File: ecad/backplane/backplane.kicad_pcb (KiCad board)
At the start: 2 copper layers, 18 parts, among them J1 10145891-0320J13LF, J2 10145891-0320J13LF, J3 10145891-0320J13LF, J4 10145891-0320J13LF, J6 USB4105-GF-A, U1 MCP16331x-xCH

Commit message: hii
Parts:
- moved R4 37.5 mm to (34.0, 106.9)
- moved J6 37.5 mm to (32.9, 115.2)
- moved R3 37.5 mm to (31.5, 106.9)
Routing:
- net GND: track 97.9 -> 112.7 mm, vias 6 -> 8
- net +5V: track 6.47 -> 18.3 mm
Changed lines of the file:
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@@
 			(effects
 				(font
-					(size 1 1)
-					(thickness 0.15)
+					(size 0.5 0.5)
+					(thickness 0.125)
 				)
 			)
@@
 			(effects
 				(font
-					(size 1 1)
-					(thickness 0.15)
+					(size 0.3 0.3)
+					(thickness 0.075)
 				)
 			)
@@
 			(effects
 				(font
-					(size 1 1)
-					(thickness 0.15)
+					(size 0.3 0.3)
+					(thickness 0.075)
 				)
 			)
@@
 			(effects
 				(font
-					(size 1 1)
-					(thickness 0.15)
+					(size 0.3 0.3)
+					(thickness 0.075)
 				)
 			)
@@
 			(effects
 				(font
-					(size 1 1)
-					(thickness 0.15)
+					(size 0.3 0.3)
+					(thickness 0.075)
 				)
 			)
@@
 			(effects
 				(font
-					(size 1 1)
-					(thickness 0.15)
+					(size 0.3 0.3)
+					(thickness 0.075)
 				)
 			)
@@
 	(footprint "Resistor_SMD:R_0402_1005Metric"
 		(layer "F.Cu")
-		(at 68.85 103.5 90)
+		(at 31.4625 106.87 90)
 		(descr "Resistor SMD 0402 (1005 Metric), square (rectangular) end terminal, IPC_7351 nominal, (Body size source: IPC-SM-782 page 72, https://www.pcb-3d.com/wordpress/wp-content/uploads/ipc-sm-782a_amendment_1_and_2.pdf), generated with kicad-footprint-generator")
 		(tags "resistor")
@@
 			(effects
 				(font
-					(size 1 1)
-					(thickness 0.15)
+					(size 0.3 0.3)
+					(thickness 0.075)
 				)
 			)
@@
 			(effects
 				(font
-					(size 1 1)
-					(thickness 0.15)
+					(size 0.3 0.3)
+					(thickness 0.075)
 				)
 			)
@@
 	(footprint "Resistor_SMD:R_0402_1005Metric"
 		(layer "F.Cu")
-		(at 71.4 103.5 90)
+		(at 34.0125 106.87 90)
 		(descr "Resistor SMD 0402 (1005 Metric), square (rectangular) end terminal, IPC_7351 nominal, (Body size source: IPC-SM-782 page 72, https://www.pcb-3d.com/wordpress/wp-content/uploads/ipc-sm-782a_amendment_1_and_2.pdf), generated with kicad-footprint-generator")
 		(tags "resistor")
@@
 	(footprint "Library:GCT_USB4105-GF-A"
 		(layer "F.Cu")
-		(at 70.2875 111.785)
+		(at 32.9 115.155)
 		(property "Reference" "J6"
 			(at -1.825 -8.635 0)
@@
 	)
 	(segment
+		(start 35.3 110.4)
+		(end 35.3 107.55)
+		(width 0.2)
+		(layer "F.Cu")
+		(net 898)
+	)
+	(segment
 		(start 45.3375 100.0625)
 		(end 44.2 101.2)
@@
 	)
 	(segment
-		(start 68.85 102.99)
-		(end 71.4 102.99)
+		(start 35.3 107.55)
+		(end 41.65 101.2)
+		(width 0.2)
+		(layer "F.Cu")
+		(net 898)
+	)
+	(segment
+		(start 31.4625 106.36)
+		(end 34.0125 106.36)
 		(width 0.2)
 		(layer "F.Cu")
@@
 	)
 	(segment
-		(start 67.0875 107.03)
-		(end 67.0875 104.7525)
+		(start 29.7 110.4)
+		(end 29.7 108.1225)
+		(width 0.2)
+		(layer "F.Cu")
+		(net 899)
+	)
+	(segment
+		(start 35.14 106.36)
+		(end 35.7 105.8)
+		(width 0.2)
+		(layer "F.Cu")
+		(net 899)
+	)
+	(segment
+		(start 36.1 107.95)
+		(end 36.1 110.4)
 		(width 0.2)
 		(layer "F.Cu")
@@
 	)
 	(segment
-		(start 74.0325 107.03)
-		(end 74.6075 107.605)
+		(start 36.645 110.4)
+		(end 37.22 110.975)
+		(width 0.2)
+		(layer "F.Cu")
+		(net 899)
+	)
+	(segment
+		(start 38.25 105.8)
+		(end 41.65 102.4)
 		(width 0.2)
 		(layer "F.Cu")
@@
 	)
 	(segment
-		(start 67.0875 104.7525)
-		(end 68.85 102.99)
+		(start 29.7 108.1225)
+		(end 31.4625 106.36)
 		(width 0.2)
 		(layer "F.Cu")
@@
 	)
 	(segment
-		(start 65.9675 107.605)
-		(end 66.5125 107.605)
+		(start 28.58 110.975)
+		(end 29.125 110.975)
 		(width 0.2)
 		(layer "F.Cu")
@@
 	)
 	(segment
-		(start 73.4875 107.03)
-		(end 74.0325 107.03)
+		(start 36.1 110.4)
+		(end 36.645 110.4)
 		(width 0.2)
 		(layer "F.Cu")
@@
 	)
 	(segment
+		(start 41.65 102.4)
+		(end 41.65 102.335)
+		(width 0.2)
+		(layer "F.Cu")
+		(net 899)
+	)
+	(segment
 		(start 46.515 104.65)
 		(end 44.2 102.335)
@@
 	)
 	(segment
-		(start 66.5125 107.605)
-		(end 67.0875 107.03)
+		(start 38.25 105.8)
+		(end 36.1 107.95)
+		(width 0.2)
+		(layer "F.Cu")
+		(net 899)
+	)
+	(segment
+		(start 34.0125 106.36)
+		(end 35.14 106.36)
+		(width 0.2)
+		(layer "F.Cu")
+		(net 899)
+	)
+	(segment
+		(start 29.125 110.975)
+		(end 29.7 110.4)
 		(width 0.2)
 		(layer "F.Cu")
@@
 	)
 	(via
+		(at 38.25 105.8)
+		(size 0.6)
+		(drill 0.3)
+		(layers "F.Cu" "B.Cu")
+		(net 899)
+	)
+	(via
 		(at 49.3 100.05)
 		(size 0.6)
@@
 	)
 	(via
+		(at 35.7 105.8)
+		(size 0.6)
+		(drill 0.3)
+		(layers "F.Cu" "B.Cu")
+		(net 899)
+	)
+	(via
 		(at 64.6 83.95)
 		(size 0.6)
@@
 	)
 	(segment
+		(start 35.7 105.8)
+		(end 38.25 105.8)
+		(width 0.2)
+		(layer "B.Cu")
+		(net 899)
+	)
+	(segment
 		(start 64.6 35.65)
 		(end 64.6 51.75)
@@
 	)
 	(segment
-		(start 69.5375 107.03)
-		(end 69.5375 104.6975)
+		(start 32.15 110.4)
+		(end 32.15 108.0675)
 		(width 0.2)
 		(layer "F.Cu")
@@
 	)
 	(segment
-		(start 69.5375 104.6975)
-		(end 68.85 104.01)
+		(start 32.15 108.0675)
+		(end 31.4625 107.38)
 		(width 0.2)
 		(layer "F.Cu")
@@
 	)
 	(segment
-		(start 71.0375 107.03)
-		(end 71.0375 104.3725)
+		(start 33.65 110.4)
+		(end 33.65 107.7425)
 		(width 0.2)
 		(layer "F.Cu")
@@
 	)
 	(segment
-		(start 71.0375 104.3725)
-		(end 71.4 104.01)
+		(start 33.65 107.7425)
+		(end 34.0125 107.38)
 		(width 0.2)
 		(layer "F.Cu")
@@
 		(min_thickness 0.25)
 		(filled_areas_thickness no)
-		(fill yes
+		(fill
 			(thermal_gap 0.5)
 			(thermal_bridge_width 0.5)
@@
 		(polygon
 			(pts
-				(xy 198.05 19.55) (xy 23.8 20.7) (xy 22.95 109.25) (xy 22.95 117.3) (xy 198.05 116.15)
+				(xy 191.25 20.7) (xy 23.8 20.7) (xy 22.95 109.25) (xy 22.95 117.3) (xy 191.25 117.3)
 			)
 		)

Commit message: various changes
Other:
- board outline added: 220 x 160 mm
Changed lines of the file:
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@@
 		)
+	)
+	(gr_rect
+		(start -5.1 -27.45)
+		(end 214.9 132.55)
+		(stroke
+			(width 0.2)
+			(type default)
+		)
+		(fill none)
+		(layer "Edge.Cuts")
 	)
 	(segment

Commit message: fix backplane pins
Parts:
- moved J6 197.6 mm to (214.0, 36.0), turned to 180 degrees
- moved R3 194.3 mm to (215.4, 44.3), turned to -90 degrees
- moved R4 189.5 mm to (212.9, 44.3), turned to -90 degrees
- moved CIn_2 171.8 mm to (205.2, 49.4), turned to 90 degrees
- moved CIn_1 166.9 mm to (202.7, 49.4), turned to 90 degrees
- moved RBot 165.0 mm to (204.4, 59.8), turned to 90 degrees
- moved C4 163.0 mm to (198.2, 43.1), turned to 0 degrees
- moved U1 161.8 mm to (201.6, 54.6), turned to 90 degrees
- moved C5 160.3 mm to (198.2, 46.5), turned to 0 degrees
- moved RTop 160.0 mm to (201.8, 59.8), turned to 90 degrees
- moved D1 154.2 mm to (196.8, 51.7), turned to 90 degrees
- moved CB 153.5 mm to (197.6, 55.8), turned to -90 degrees
- moved DB 147.0 mm to (194.2, 55.8), turned to -90 degrees
- moved L 146.1 mm to (192.5, 51.7), turned to 90 degrees
- moved J1 116.0 mm to (104.8, 146.8), turned to 90 degrees
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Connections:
- net /ADDR00 renamed /BUS42
- net /ADDR02 renamed /BUS43
- net /ADDR04 renamed /BUS44
- net /ADDR06 renamed /BUS45
- net /ADDR08 renamed /BUS48
- net /BUS00 renamed /BUS54
- net /BUS02 renamed /BUS55
- net /BUS04 renamed /BUS56
- net /BUS15 renamed /BUS24
- net /BUS16 renamed /BUS66
- net /DATA00 renamed /BUS72
- net /DATA01 renamed /BUS33
- net /DATA03 renamed /BUS34
- net /DATA05 renamed /BUS35
- net /DATA07 renamed /BUS36
- J1 pad 10: /ADDR11 -> /BUS10
- J1 pad 11: /ADDR13 -> /BUS11
- J1 pad 12: /ADDR15 -> /BUS12
- J1 pad 14: GND -> 3.3V
- J1 pad 15: /BUS01 -> GND
- J1 pad 16: /BUS03 -> GND
- J1 pad 17: /BUS05 -> /BUS17
- J1 pad 18: /BUS07 -> /BUS18
- J1 pad 19: 3.3V -> /BUS19
- J1 pad 2: GND -> 3.3V
- J1 pad 20: GND -> /BUS20
- J1 pad 21: /BUS09 -> /BUS21
- J1 pad 22: /BUS11 -> /BUS22
- J1 pad 23: /BUS13 -> /BUS23
- J1 pad 26: GND -> 3.3V
- J1 pad 27: /BUS17 -> GND
- J1 pad 28: /BUS19 -> GND
- J1 pad 29: /BUS21 -> /BUS29
- J1 pad 3: /ADDR01 -> GND
- J1 pad 30: /BUS23 -> /BUS30
- J1 pad 31: 3.3V -> /BUS31
- J1 pad 32: GND -> /BUS32
- J1 pad 38: GND -> 3.3V
- J1 pad 39: unconnected-(J1-Pad39) -> GND
- J1 pad 4: /ADDR03 -> GND
- J1 pad 40: 3.3V -> GND
- J1 pad 41: GND -> /BUS41
- J1 pad 46: 3.3V -> /BUS46
- J1 pad 47: GND -> /BUS47
- J1 pad 49: /ADDR10 -> 3.3V
- J1 pad 5: /ADDR05 -> /BUS05
- J1 pad 50: /ADDR12 -> 3.3V
- J1 pad 51: /ADDR14 -> GND
- J1 pad 52: 3.3V -> GND
- J1 pad 53: GND -> /BUS53
- J1 pad 57: /BUS06 -> /BUS57
- J1 pad 58: 3.3V -> /BUS58
- J1 pad 59: GND -> /BUS59
- J1 pad 6: /ADDR07 -> /BUS06
- J1 pad 60: /BUS08 -> /BUS60
- J1 pad 61: /BUS10 -> 3.3V
- J1 pad 62: /BUS12 -> 3.3V
- J1 pad 63: /BUS14 -> GND
- J1 pad 64: 3.3V -> GND
- J1 pad 65: GND -> /BUS65
- J1 pad 67: /BUS18 -> /BUS67
- J1 pad 68: /BUS20 -> /BUS68
- J1 pad 69: /BUS22 -> /BUS69
- J1 pad 7: 3.3V -> /BUS07
- J1 pad 70: 3.3V -> /BUS70
- J1 pad 71: GND -> /BUS71
- J1 pad 73: /DATA02 -> 3.3V
- J1 pad 74: /DATA04 -> 3.3V
- J1 pad 75: /DATA06 -> GND
- J1 pad 76: 3.3V -> GND
- J1 pad 77: GND -> unconnected-(J1-Pad77)
- J1 pad 8: GND -> /BUS08
- J1 pad 9: /ADDR09 -> /BUS09
- J2 pad 10: /ADDR11 -> /BUS10
- J2 pad 11: /ADDR13 -> /BUS11
- J2 pad 12: /ADDR15 -> /BUS12
- J2 pad 14: GND -> 3.3V
- J2 pad 15: /BUS01 -> GND
- J2 pad 16: /BUS03 -> GND
- J2 pad 17: /BUS05 -> /BUS17
- J2 pad 18: /BUS07 -> /BUS18
- J2 pad 19: 3.3V -> /BUS19
- J2 pad 2: GND -> 3.3V
- J2 pad 20: GND -> /BUS20
- J2 pad 21: /BUS09 -> /BUS21
- J2 pad 22: /BUS11 -> /BUS22
- J2 pad 23: /BUS13 -> /BUS23
- J2 pad 26: GND -> 3.3V
- J2 pad 27: /BUS17 -> GND
- J2 pad 28: /BUS19 -> GND
- J2 pad 29: /BUS21 -> /BUS29
- J2 pad 3: /ADDR01 -> GND
- J2 pad 30: /BUS23 -> /BUS30
- J2 pad 31: 3.3V -> /BUS31
- J2 pad 32: GND -> /BUS32
- J2 pad 38: GND -> 3.3V
- J2 pad 39: unconnected-(J2-Pad39) -> GND
- J2 pad 4: /ADDR03 -> GND
- J2 pad 40: 3.3V -> GND
- J2 pad 41: GND -> /BUS41
- J2 pad 46: 3.3V -> /BUS46
- J2 pad 47: GND -> /BUS47
- J2 pad 49: /ADDR10 -> 3.3V
- J2 pad 5: /ADDR05 -> /BUS05
- J2 pad 50: /ADDR12 -> 3.3V
- J2 pad 51: /ADDR14 -> GND
- J2 pad 52: 3.3V -> GND
- J2 pad 53: GND -> /BUS53
- J2 pad 57: /BUS06 -> /BUS57
- J2 pad 58: 3.3V -> /BUS58
- J2 pad 59: GND -> /BUS59
- J2 pad 6: /ADDR07 -> /BUS06
- J2 pad 60: /BUS08 -> /BUS60
- J2 pad 61: /BUS10 -> 3.3V
- J2 pad 62: /BUS12 -> 3.3V
- J2 pad 63: /BUS14 -> GND
- J2 pad 64: 3.3V -> GND
- J2 pad 65: GND -> /BUS65
- J2 pad 67: /BUS18 -> /BUS67
- J2 pad 68: /BUS20 -> /BUS68
- J2 pad 69: /BUS22 -> /BUS69
- J2 pad 7: 3.3V -> /BUS07
- J2 pad 70: 3.3V -> /BUS70
- J2 pad 71: GND -> /BUS71
- J2 pad 73: /DATA02 -> 3.3V
- J2 pad 74: /DATA04 -> 3.3V
- J2 pad 75: /DATA06 -> GND
- J2 pad 76: 3.3V -> GND
- J2 pad 77: GND -> unconnected-(J2-Pad77)
- J2 pad 8: GND -> /BUS08
- J2 pad 9: /ADDR09 -> /BUS09
- J3 pad 10: /ADDR11 -> /BUS10
- J3 pad 11: /ADDR13 -> /BUS11
- J3 pad 12: /ADDR15 -> /BUS12
- J3 pad 14: GND -> 3.3V
- J3 pad 15: /BUS01 -> GND
- J3 pad 16: /BUS03 -> GND
- J3 pad 17: /BUS05 -> /BUS17
- J3 pad 18: /BUS07 -> /BUS18
- J3 pad 19: 3.3V -> /BUS19
- J3 pad 2: GND -> 3.3V
- J3 pad 20: GND -> /BUS20
- J3 pad 21: /BUS09 -> /BUS21
- J3 pad 22: /BUS11 -> /BUS22
- J3 pad 23: /BUS13 -> /BUS23
- J3 pad 26: GND -> 3.3V
- J3 pad 27: /BUS17 -> GND
- J3 pad 28: /BUS19 -> GND
- J3 pad 29: /BUS21 -> /BUS29
- J3 pad 3: /ADDR01 -> GND
- J3 pad 30: /BUS23 -> /BUS30
- J3 pad 31: 3.3V -> /BUS31
- J3 pad 32: GND -> /BUS32
- J3 pad 38: GND -> 3.3V
- J3 pad 39: unconnected-(J3-Pad39) -> GND
- J3 pad 4: /ADDR03 -> GND
- J3 pad 40: 3.3V -> GND
- J3 pad 41: GND -> /BUS41
- J3 pad 46: 3.3V -> /BUS46
- J3 pad 47: GND -> /BUS47
- J3 pad 49: /ADDR10 -> 3.3V
- J3 pad 5: /ADDR05 -> /BUS05
- J3 pad 50: /ADDR12 -> 3.3V
- J3 pad 51: /ADDR14 -> GND
- J3 pad 52: 3.3V -> GND
- J3 pad 53: GND -> /BUS53
- J3 pad 57: /BUS06 -> /BUS57
- J3 pad 58: 3.3V -> /BUS58
- J3 pad 59: GND -> /BUS59
- J3 pad 6: /ADDR07 -> /BUS06
- J3 pad 60: /BUS08 -> /BUS60
- J3 pad 61: /BUS10 -> 3.3V
- J3 pad 62: /BUS12 -> 3.3V
- J3 pad 63: /BUS14 -> GND
- J3 pad 64: 3.3V -> GND
- J3 pad 65: GND -> /BUS65
- J3 pad 67: /BUS18 -> /BUS67
- J3 pad 68: /BUS20 -> /BUS68
- J3 pad 69: /BUS22 -> /BUS69
- J3 pad 7: 3.3V -> /BUS07
- J3 pad 70: 3.3V -> /BUS70
- J3 pad 71: GND -> /BUS71
- J3 pad 73: /DATA02 -> 3.3V
- J3 pad 74: /DATA04 -> 3.3V
- J3 pad 75: /DATA06 -> GND
- J3 pad 76: 3.3V -> GND
- J3 pad 77: GND -> unconnected-(J3-Pad77)
- J3 pad 8: GND -> /BUS08
- J3 pad 9: /ADDR09 -> /BUS09
- J4 pad 10: /ADDR11 -> /BUS10
- J4 pad 11: /ADDR13 -> /BUS11
- J4 pad 12: /ADDR15 -> /BUS12
- J4 pad 14: GND -> 3.3V
- J4 pad 15: /BUS01 -> GND
- J4 pad 16: /BUS03 -> GND
- J4 pad 17: /BUS05 -> /BUS17
- J4 pad 18: /BUS07 -> /BUS18
- J4 pad 19: 3.3V -> /BUS19
- J4 pad 2: GND -> 3.3V
- J4 pad 20: GND -> /BUS20
- J4 pad 21: /BUS09 -> /BUS21
- J4 pad 22: /BUS11 -> /BUS22
- J4 pad 23: /BUS13 -> /BUS23
- J4 pad 26: GND -> 3.3V
- J4 pad 27: /BUS17 -> GND
- J4 pad 28: /BUS19 -> GND
- J4 pad 29: /BUS21 -> /BUS29
- J4 pad 3: /ADDR01 -> GND
- J4 pad 30: /BUS23 -> /BUS30
- J4 pad 31: 3.3V -> /BUS31
- J4 pad 32: GND -> /BUS32
- J4 pad 38: GND -> 3.3V
- J4 pad 39: unconnected-(J4-Pad39) -> GND
- J4 pad 4: /ADDR03 -> GND
- J4 pad 40: 3.3V -> GND
- J4 pad 41: GND -> /BUS41
- J4 pad 46: 3.3V -> /BUS46
- J4 pad 47: GND -> /BUS47
- J4 pad 49: /ADDR10 -> 3.3V
- J4 pad 5: /ADDR05 -> /BUS05
- J4 pad 50: /ADDR12 -> 3.3V
- J4 pad 51: /ADDR14 -> GND
- J4 pad 52: 3.3V -> GND
- J4 pad 53: GND -> /BUS53
- J4 pad 57: /BUS06 -> /BUS57
- J4 pad 58: 3.3V -> /BUS58
- J4 pad 59: GND -> /BUS59
- J4 pad 6: /ADDR07 -> /BUS06
- J4 pad 60: /BUS08 -> /BUS60
- J4 pad 61: /BUS10 -> 3.3V
- J4 pad 62: /BUS12 -> 3.3V
- J4 pad 63: /BUS14 -> GND
- J4 pad 64: 3.3V -> GND
- J4 pad 65: GND -> /BUS65
- J4 pad 67: /BUS18 -> /BUS67
- J4 pad 68: /BUS20 -> /BUS68
- J4 pad 69: /BUS22 -> /BUS69
- J4 pad 7: 3.3V -> /BUS07
- J4 pad 70: 3.3V -> /BUS70
- J4 pad 71: GND -> /BUS71
- J4 pad 73: /DATA02 -> 3.3V
- J4 pad 74: /DATA04 -> 3.3V
- J4 pad 75: /DATA06 -> GND
- J4 pad 76: 3.3V -> GND
- J4 pad 77: GND -> unconnected-(J4-Pad77)
- J4 pad 8: GND -> /BUS08
- J4 pad 9: /ADDR09 -> /BUS09
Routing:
- net GND: track 112.7 -> 572.7 mm, vias 8 -> 40
- net 3.3V: track 83.2 -> 485.7 mm, vias 4 -> 32
- net /BUS67: track 0.00 -> 115.0 mm, vias 0 -> 8
- net /BUS69: track 0.00 -> 57.5 mm, vias 0 -> 4
- net /BUS68: track 0.00 -> 57.5 mm, vias 0 -> 4
- net /BUS60: track 0.00 -> 57.5 mm, vias 0 -> 4
- net /BUS57: track 0.00 -> 57.5 mm, vias 0 -> 4
- net /BUS30: track 0.00 -> 57.5 mm, vias 0 -> 4
- net /BUS29: track 0.00 -> 57.5 mm, vias 0 -> 4
- net /DATA06: track 57.5 -> 0.00 mm, vias 4 -> 0
- net /DATA04: track 57.5 -> 0.00 mm, vias 4 -> 0
- net /DATA02: track 57.5 -> 0.00 mm, vias 4 -> 0
- net /BUS20: track 57.5 -> 0.00 mm, vias 4 -> 0
- net /BUS19: track 57.5 -> 0.00 mm, vias 4 -> 0
- net /BUS14: track 57.5 -> 0.00 mm, vias 4 -> 0
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- removed copper zone on B.Cu, net GND
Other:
- board outline removed

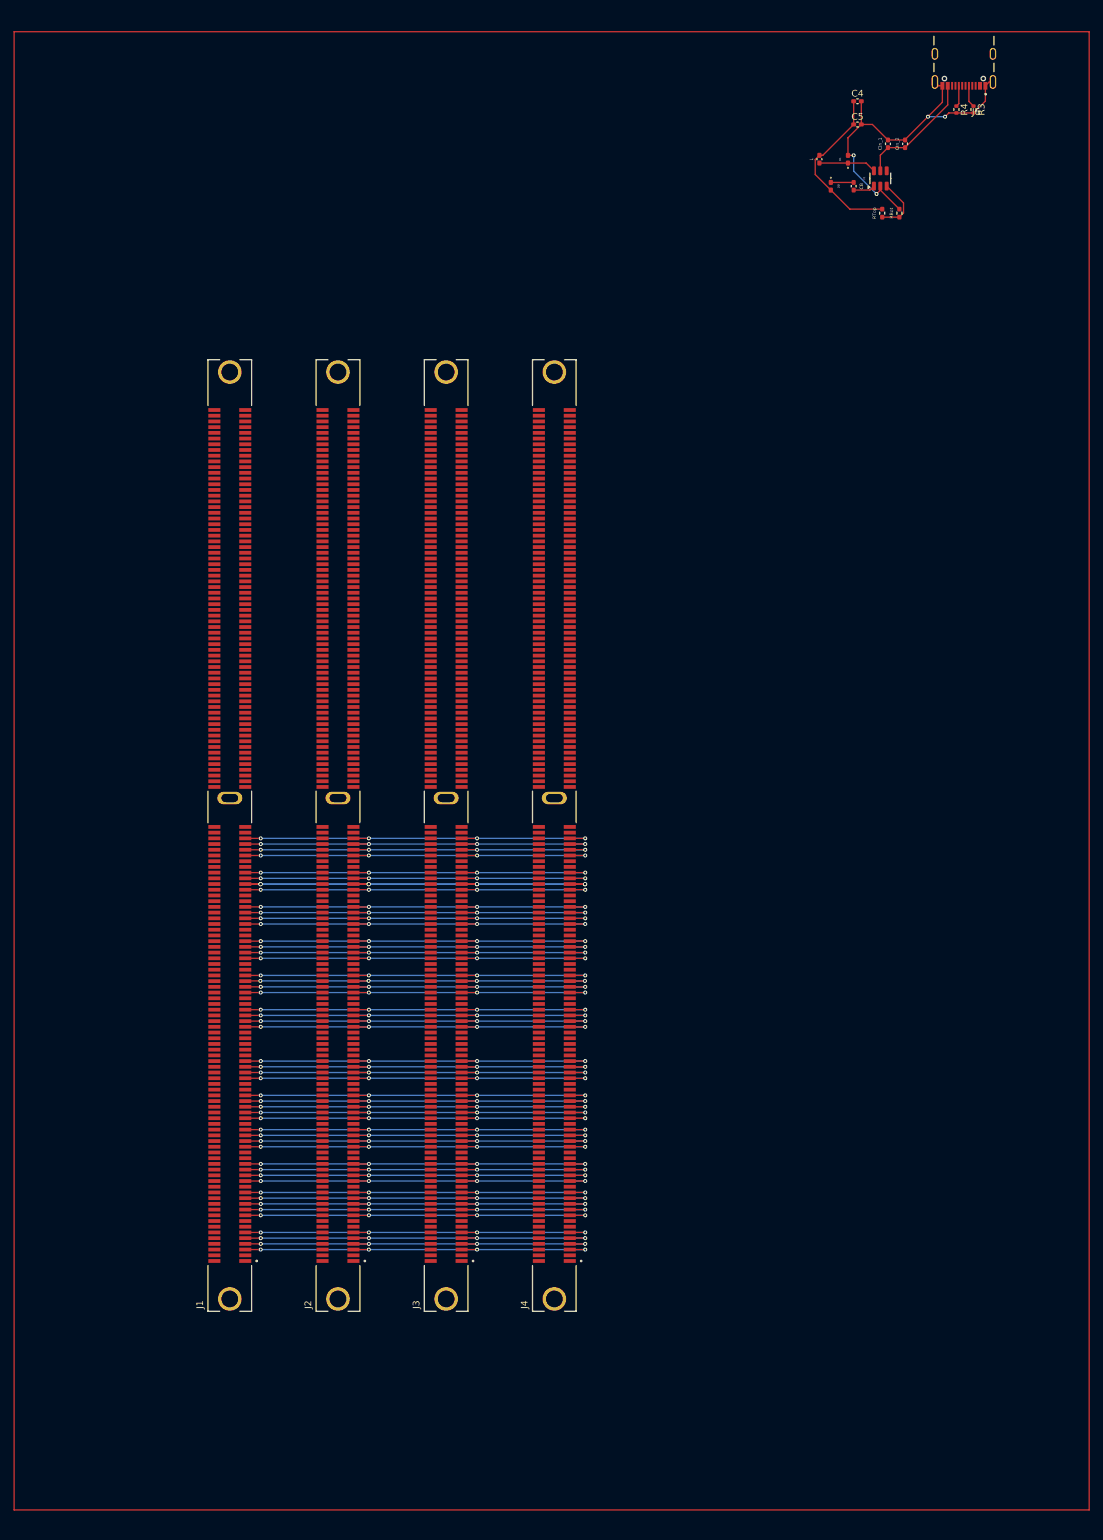
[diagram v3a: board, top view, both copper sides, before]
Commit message: more backplane. add nathan's panel changes
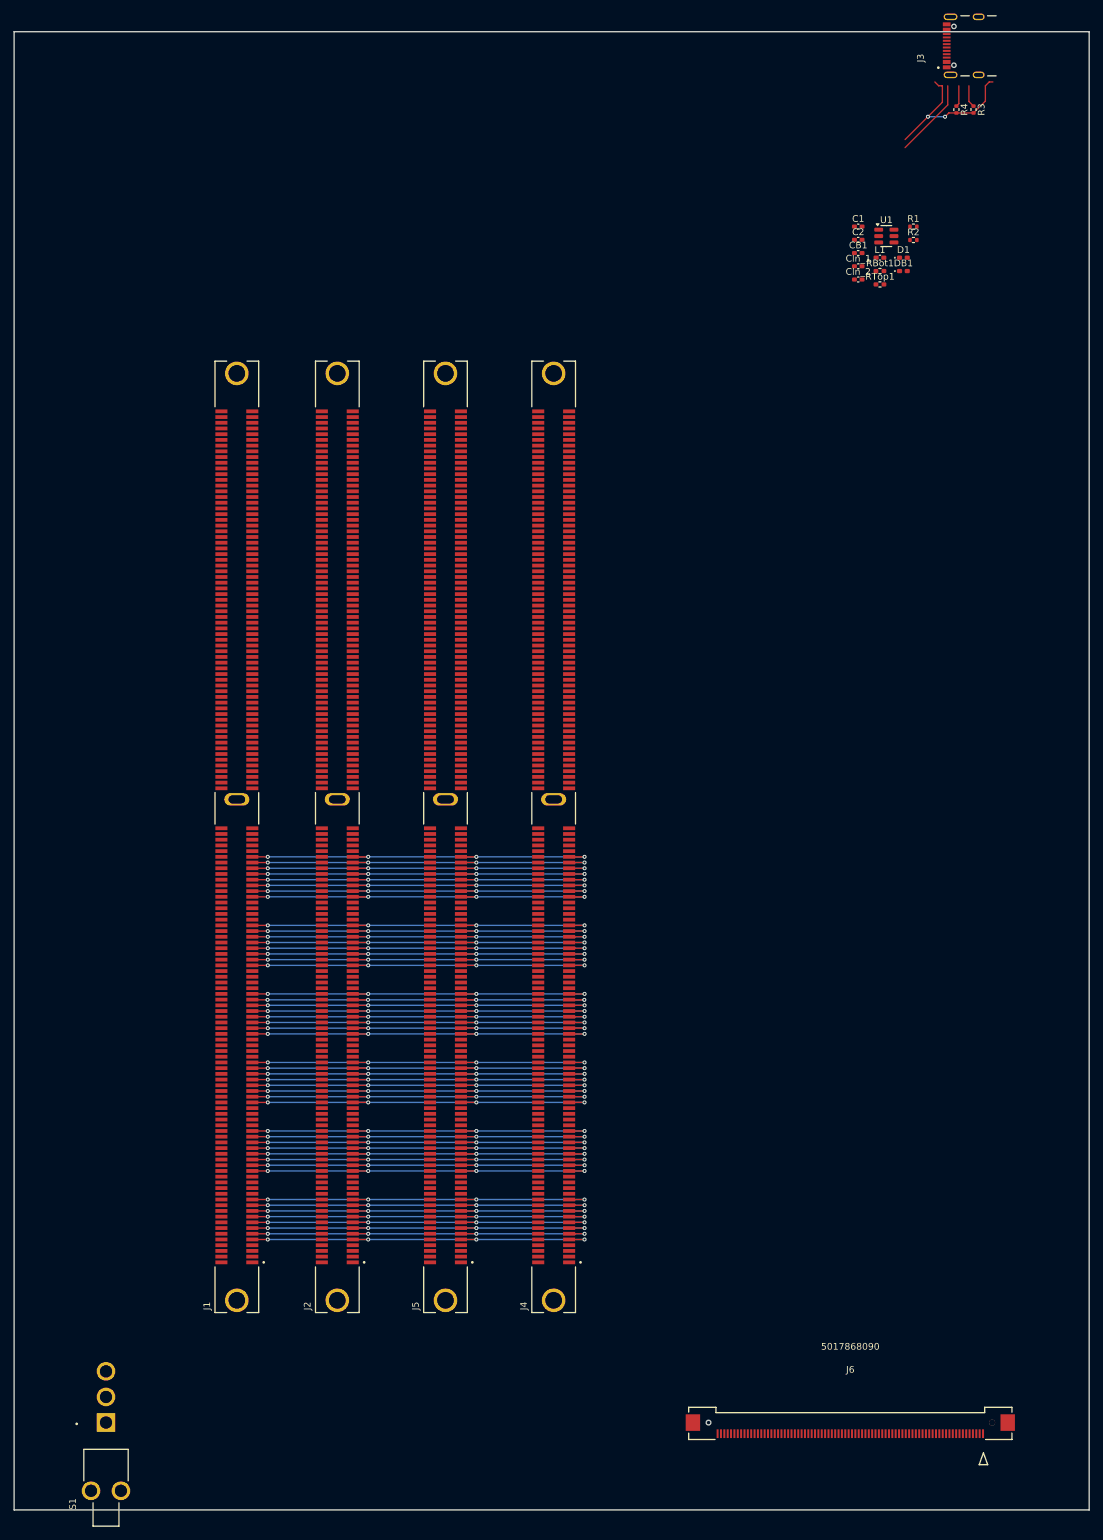
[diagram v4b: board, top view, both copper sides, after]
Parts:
- removed C4, C5, CIn_1, CIn_2: 10u, Capacitor_SMD:C_0402_1005Metric_Pad0.74x0.62mm_HandSolder
- removed CB: 100n, Capacitor_SMD:C_0402_1005Metric_Pad0.74x0.62mm_HandSolder
- removed DB: 1N4148, Diode_SMD:D_0402_1005Metric_Pad0.77x0.64mm_HandSolder
- removed L: 15u, Inductor_SMD:L_0402_1005Metric_Pad0.77x0.64mm_HandSolder
- removed RBot: 10k, Resistor_SMD:R_0402_1005Metric_Pad0.72x0.64mm_HandSolder
- removed RTop: 31.6k, Resistor_SMD:R_0402_1005Metric_Pad0.72x0.64mm_HandSolder
- added C1: 10u, Capacitor_SMD:C_0402_1005Metric_Pad0.74x0.62mm_HandSolder, F.Cu at (198.3, 61.8)
- added C2: 10u, Capacitor_SMD:C_0402_1005Metric_Pad0.74x0.62mm_HandSolder, F.Cu at (198.3, 63.7)
- added CB1: 100n, Capacitor_SMD:C_0402_1005Metric_Pad0.74x0.62mm_HandSolder, F.Cu at (198.3, 65.7)
- added Cln_1: 10u, Capacitor_SMD:C_0402_1005Metric_Pad0.74x0.62mm_HandSolder, F.Cu at (198.3, 67.7)
- added Cln_2: 10u, Capacitor_SMD:C_0402_1005Metric_Pad0.74x0.62mm_HandSolder, F.Cu at (198.3, 69.6)
- added DB1: 1N4148, Diode_SMD:D_0402_1005Metric_Pad0.77x0.64mm_HandSolder, F.Cu at (205.0, 68.4)
- added J5: 10145891-0320J13LF, Library:AMPHENOL_10145891-0320J13LF, F.Cu at (136.8, 147.0)
- added L1: 15u, Inductor_SMD:L_0402_1005Metric_Pad0.77x0.64mm_HandSolder, F.Cu at (201.5, 66.4)
- added R1: 5.1k, Resistor_SMD:R_0402_1005Metric, F.Cu at (206.5, 61.8)
- added R2: 5.1k, Resistor_SMD:R_0402_1005Metric, F.Cu at (206.5, 63.8)
- added RBot1: 10k, Resistor_SMD:R_0402_1005Metric_Pad0.72x0.64mm_HandSolder, F.Cu at (201.5, 68.4)
- added RTop1: 31.6k, Resistor_SMD:R_0402_1005Metric_Pad0.72x0.64mm_HandSolder, F.Cu at (201.5, 70.4)
- added S1: 500SSP1S1M7QEA, Library:SW_500SSP1S1M7QEA, F.Cu at (86.3, 242.9)
- D1: value 1N4148 -> D_Schottky
- J3: value 10145891-0320J13LF -> USB4105-GF-A; footprint Library:AMPHENOL_10145891-0320J13LF -> Library:GCT_USB4105-GF-A
- J6: value USB4105-GF-A -> 5017868090; footprint Library:GCT_USB4105-GF-A -> Library:CON_5017868090
- moved J6 204.4 mm to (197.1, 239.8), turned to 0 degrees
- moved J3 137.2 mm to (216.2, 34.9)
- moved D1 16.8 mm to (205.0, 66.4), turned to 0 degrees
- moved U1 8.62 mm to (202.5, 63.2), turned to 0 degrees
- moved J1 1.07 mm to (105.8, 147.0)
- moved J4 0.22 mm to (152.9, 147.0)
- moved J2 0.22 mm to (120.8, 147.0)
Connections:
- D1 pad 2: 3.3V -> GND
- U1 pad 6: Net-(D2-K) -> Net-(D1-K)
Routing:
- net GND: track 572.7 -> 24.8 mm, vias 40 -> 2
- net 3.3V: track 485.7 -> 0.00 mm, vias 32 -> 0
- net /BUS67: track 115.0 -> 56.4 mm, vias 8 -> 4
- net /BUS71: track 0.00 -> 56.4 mm, vias 0 -> 4
- net /BUS70: track 0.00 -> 56.4 mm, vias 0 -> 4
- net /BUS65: track 0.00 -> 56.4 mm, vias 0 -> 4
- net /BUS59: track 0.00 -> 56.4 mm, vias 0 -> 4
- net /BUS58: track 0.00 -> 56.4 mm, vias 0 -> 4
- net /BUS53: track 0.00 -> 56.4 mm, vias 0 -> 4
- net /BUS46: track 0.00 -> 56.4 mm, vias 0 -> 4
- net /BUS41: track 0.00 -> 56.4 mm, vias 0 -> 4
- net /BUS32: track 0.00 -> 56.4 mm, vias 0 -> 4
- net /BUS31: track 0.00 -> 56.4 mm, vias 0 -> 4
- net /BUS20: track 0.00 -> 56.4 mm, vias 0 -> 4
- net /BUS19: track 0.00 -> 56.4 mm, vias 0 -> 4
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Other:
- board outline added: 160 x 220 mm
